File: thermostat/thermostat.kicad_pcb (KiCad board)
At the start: 2 copper layers, 13 parts, among them J1 Wall connections, J2 UART, U1 ESP32-WROVER-E, U2 TPS5430DDA, U3 TPS62203DBV

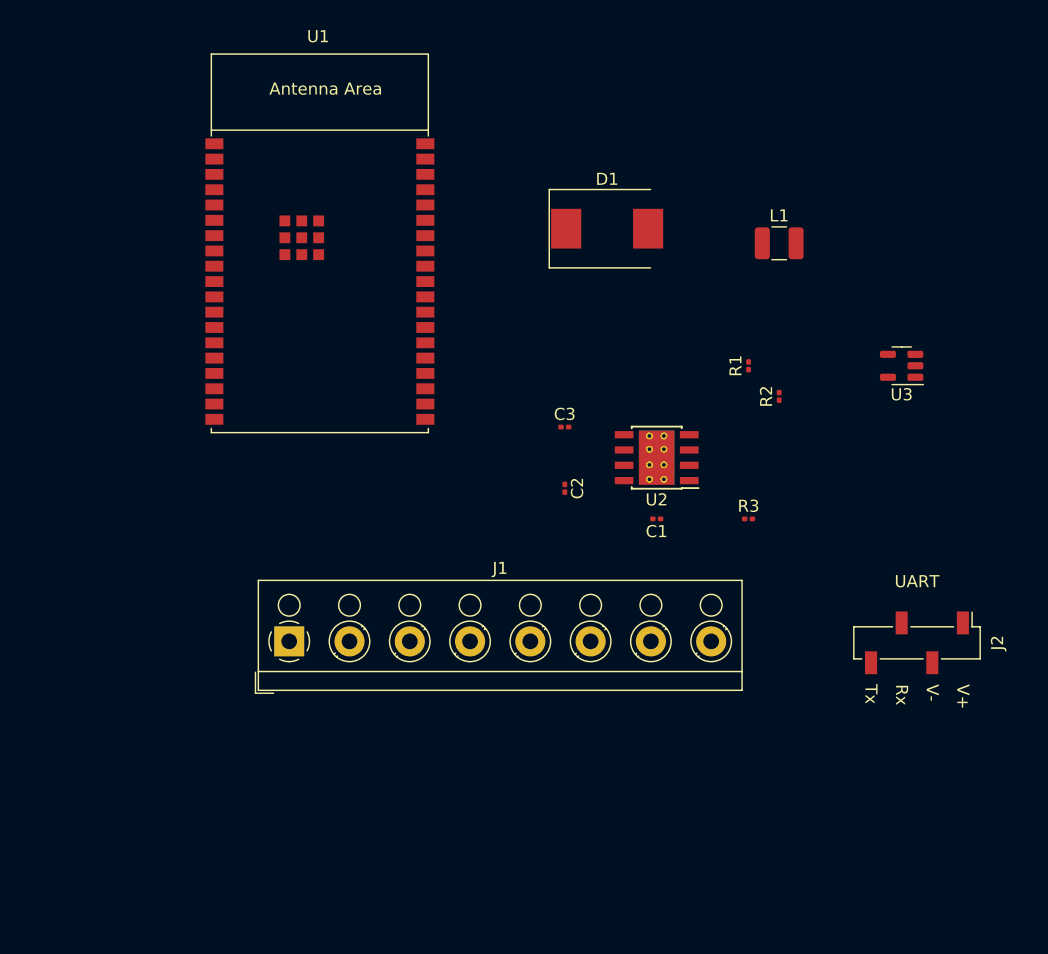
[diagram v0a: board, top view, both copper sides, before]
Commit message: update thermostat
I think I chose all the parts, just need to optimize the layout
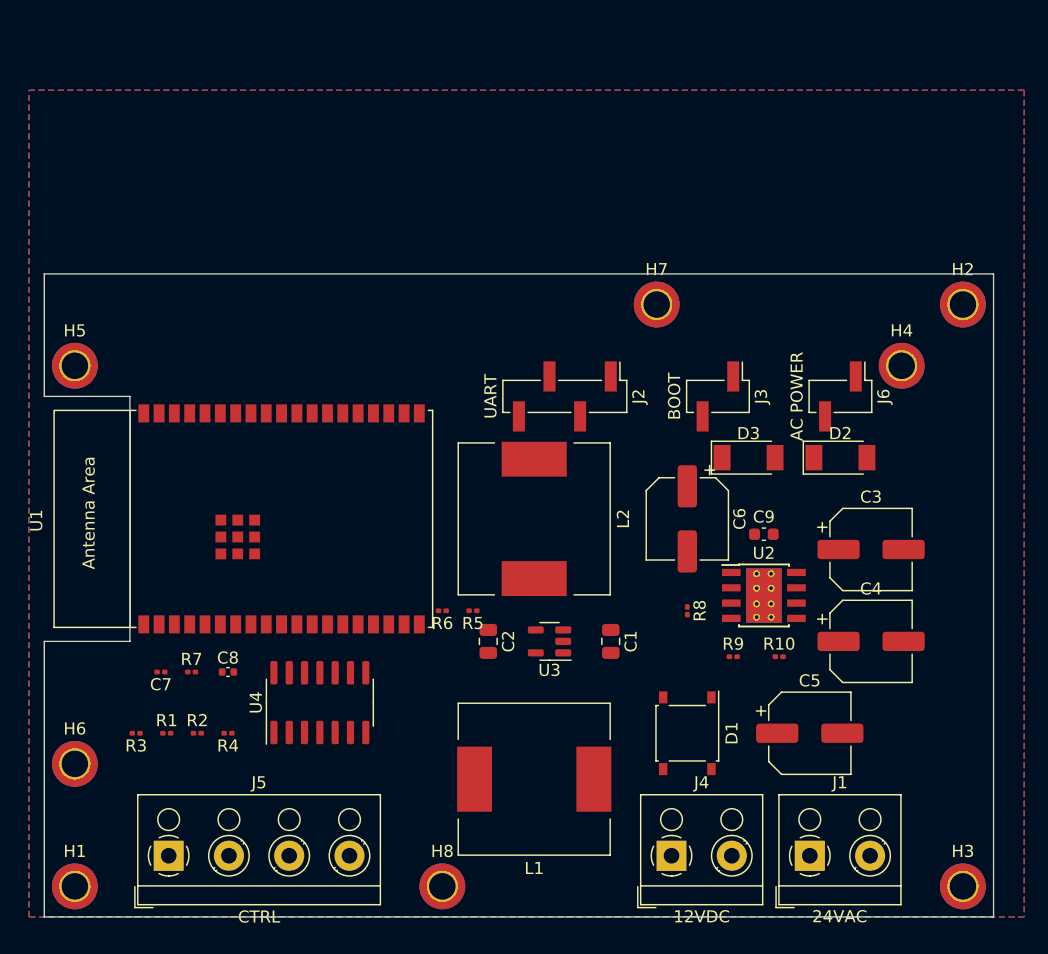
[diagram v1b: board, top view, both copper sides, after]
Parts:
- added C4: 470uF/50V, Capacitor_SMD:CP_Elec_6.3x7.7, F.Cu at (134.6, 121.9)
- added C5: 470uF/50V, Capacitor_SMD:CP_Elec_6.3x7.7, F.Cu at (129.5, 129.5)
- added C6: 100uF/25V, Capacitor_SMD:CP_Elec_6.3x7.7, F.Cu at (119.4, 111.8)
- added C7: 0.1uF/5V, Capacitor_SMD:C_0201_0603Metric, F.Cu at (75.7, 124.5)
- added C8: 1uF/5V, Capacitor_SMD:C_0402_1005Metric, F.Cu at (81.3, 124.5)
- added C9: 0.01uF, Capacitor_SMD:C_0603_1608Metric, F.Cu at (125.7, 113.0)
- added D2: SS34, Diode_SMD:D_SOD-128, F.Cu at (132.1, 106.7)
- added D3: SS34, Diode_SMD:D_SOD-128, F.Cu at (124.5, 106.7)
- added H1: MountingHole_Pad, MountingHole:MountingHole_2.2mm_M2_DIN965_Pad_TopBottom, F.Cu at (68.6, 142.2)
- added H2: MountingHole_Pad, MountingHole:MountingHole_2.2mm_M2_DIN965_Pad_TopBottom, F.Cu at (142.2, 94.0)
- added H3: MountingHole_Pad, MountingHole:MountingHole_2.2mm_M2_DIN965_Pad_TopBottom, F.Cu at (142.2, 142.2)
- added H4: MountingHole_Pad, MountingHole:MountingHole_2.2mm_M2_DIN965_Pad_TopBottom, F.Cu at (137.2, 99.1)
- added H5: MountingHole_Pad, MountingHole:MountingHole_2.2mm_M2_DIN965_Pad_TopBottom, F.Cu at (68.6, 99.1)
- added H6: MountingHole_Pad, MountingHole:MountingHole_2.2mm_M2_DIN965_Pad_TopBottom, F.Cu at (68.6, 132.1)
- added H7: MountingHole_Pad, MountingHole:MountingHole_2.2mm_M2_DIN965_Pad_TopBottom, F.Cu at (116.8, 94.0)
- added H8: MountingHole_Pad, MountingHole:MountingHole_2.2mm_M2_DIN965_Pad_TopBottom, F.Cu at (99.1, 142.2)
- added J3: BOOT, Connector_PinHeader_2.54mm:PinHeader_1x02_P2.54mm_Vertical_SMD_Pin1Left, F.Cu at (121.9, 101.6)
- added J4: 12VDC, TerminalBlock_RND:TerminalBlock_RND_205-00001_1x02_P5.00mm_Horizontal, F.Cu at (118.1, 139.7)
- added J5: CTRL, TerminalBlock_RND:TerminalBlock_RND_205-00003_1x04_P5.00mm_Horizontal, F.Cu at (76.4, 139.7)
- added J6: AC POWER, Connector_PinHeader_2.54mm:PinHeader_1x02_P2.54mm_Vertical_SMD_Pin1Left, F.Cu at (132.1, 101.6)
- added L2: YPRH1207-270M, Inductor_SMD:L_12x12mm_H8mm, F.Cu at (106.7, 111.8)
- added R10: 1.8k, Resistor_SMD:R_0201_0603Metric, F.Cu at (127.0, 123.2)
- added R4: 68k, Resistor_SMD:R_0201_0603Metric, F.Cu at (81.3, 129.5)
- added R5: 18k, Resistor_SMD:R_0201_0603Metric, F.Cu at (101.6, 119.4)
- added R6: 2k, Resistor_SMD:R_0201_0603Metric, F.Cu at (99.1, 119.4)
- added R7: 10k, Resistor_SMD:R_0201_0603Metric, F.Cu at (78.3, 124.5)
- added R8: 33k, Resistor_SMD:R_0201_0603Metric, F.Cu at (119.4, 119.4)
- added R9: 1.8k, Resistor_SMD:R_0201_0603Metric, F.Cu at (123.2, 123.2)
- added U4: LM324DT, Package_SO:SOIC-14_3.9x8.7mm_P1.27mm, F.Cu at (88.9, 127.0)
- C1: value 0.01uF -> 4.7 uF; footprint Capacitor_SMD:C_0201_0603Metric -> Capacitor_SMD:C_0805_2012Metric
- C2: value 10uF -> 10 uF; footprint Capacitor_SMD:C_0201_0603Metric -> Capacitor_SMD:C_0805_2012Metric
- C3: value 220uF -> 470uF/50V; footprint Capacitor_SMD:C_0201_0603Metric -> Capacitor_SMD:CP_Elec_6.3x7.7
- D1: value B340 -> ABS2; footprint Diode_SMD:D_SMC -> Diode_SMD:Diode_Bridge_Diotec_ABS
- J1: value Wall connections -> 24VAC; footprint TerminalBlock_RND:TerminalBlock_RND_205-00007_1x08_P5.00mm_Horizontal -> TerminalBlock_RND:TerminalBlock_RND_205-00001_1x02_P5.00mm_Horizontal
- J2: footprint Connector_PinSocket_2.54mm:PinSocket_1x04_P2.54mm_Vertical_SMD_Pin1Left -> Connector_PinHeader_2.54mm:PinHeader_1x04_P2.54mm_Vertical_SMD_Pin1Left
- L1: value 15uH -> YPRH1207-270M; footprint Inductor_SMD:L_1210_3225Metric -> Inductor_SMD:L_12x12mm_H8mm
- R1: value 10k -> 33k
- R2: value 1.37k -> 33k
- R3: value 20 -> 68k
- moved R1 57.1 mm to (76.2, 129.5), turned to 0 degrees
- moved R2 55.8 mm to (78.7, 129.5), turned to 0 degrees
- moved R3 53.8 mm to (73.7, 129.5), turned to 180 degrees
- moved L1 48.9 mm to (106.7, 133.3), turned to 180 degrees
- moved J1 46.7 mm to (129.5, 139.7)
- moved D1 42.4 mm to (119.4, 129.5), turned to -90 degrees
- moved U3 37.1 mm to (108.0, 121.9)
- moved J2 35.7 mm to (109.2, 101.6)
- moved C3 27.4 mm to (134.6, 114.3)
- moved U1 23.7 mm to (82.5, 111.8), turned to 90 degrees
- moved U2 14.5 mm to (125.7, 118.1), turned to 0 degrees
- moved C2 14.2 mm to (102.9, 121.9)
- moved C1 10.9 mm to (113.0, 121.9), turned to -90 degrees
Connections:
- C1 pad 1: Net-(C1-Pad1) -> /VCC12
- C1 pad 2: Net-(C1-Pad2) -> GND
- C2 pad 1: +12V -> /VCC33
- C3 pad 1: /VCC10 -> Net-(C3-Pad1)
- D1 pad 1: Net-(C1-Pad2) -> Net-(C3-Pad1)
- J1 pad 1: GND -> /VAC-
- J1 pad 2: +12V -> /VAC+
- J2 pad 1: /VCC33_IN -> /VCC33
- L1 pad 1: Net-(C1-Pad2) -> Net-(L1-Pad1)
- L1 pad 2: /VCC10 -> /VCC33
- R1 pad 2: /VCC10 -> GND
- R2 pad 1: Net-(R1-Pad1) -> Net-(R2-Pad1)
- R2 pad 2: Net-(R2-Pad2) -> GND
- R3 pad 1: Net-(R2-Pad2) -> Net-(R1-Pad1)
- R3 pad 2: GND -> /FAN_CTRL
- U1 pad 10: unconnected-(U1-Pad10) -> /GPIO25
- U1 pad 11: unconnected-(U1-Pad11) -> /GPIO26
- U1 pad 2: /VCC33_IN -> /VCC33
- U1 pad 25: unconnected-(U1-Pad25) -> /GPIO0
- U1 pad 3: unconnected-(U1-Pad3) -> /CHIP_PU
- U1 pad 35: unconnected-(U1-Pad35) -> /UART_TX
- U1 pad 4: unconnected-(U1-Pad4) -> /ADC1_CH0
- U2 pad 1: Net-(C1-Pad1) -> Net-(C9-Pad1)
- U2 pad 4: Net-(R1-Pad1) -> Net-(R8-Pad2)
- U2 pad 7: +12V -> Net-(C3-Pad1)
- U2 pad 8: Net-(C1-Pad2) -> Net-(C9-Pad2)
- U3 pad 1: +12V -> /VCC12
- U3 pad 3: unconnected-(U3-Pad3) -> /VCC12
- U3 pad 4: unconnected-(U3-Pad4) -> /VCC33
- U3 pad 5: unconnected-(U3-Pad5) -> Net-(L1-Pad1)
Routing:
- added copper zone on B.Cu, net GND
- added copper zone on F.Cu, net GND
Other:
- board outline added: 78.7 x 53.3 mm
- board text removed: "UART"

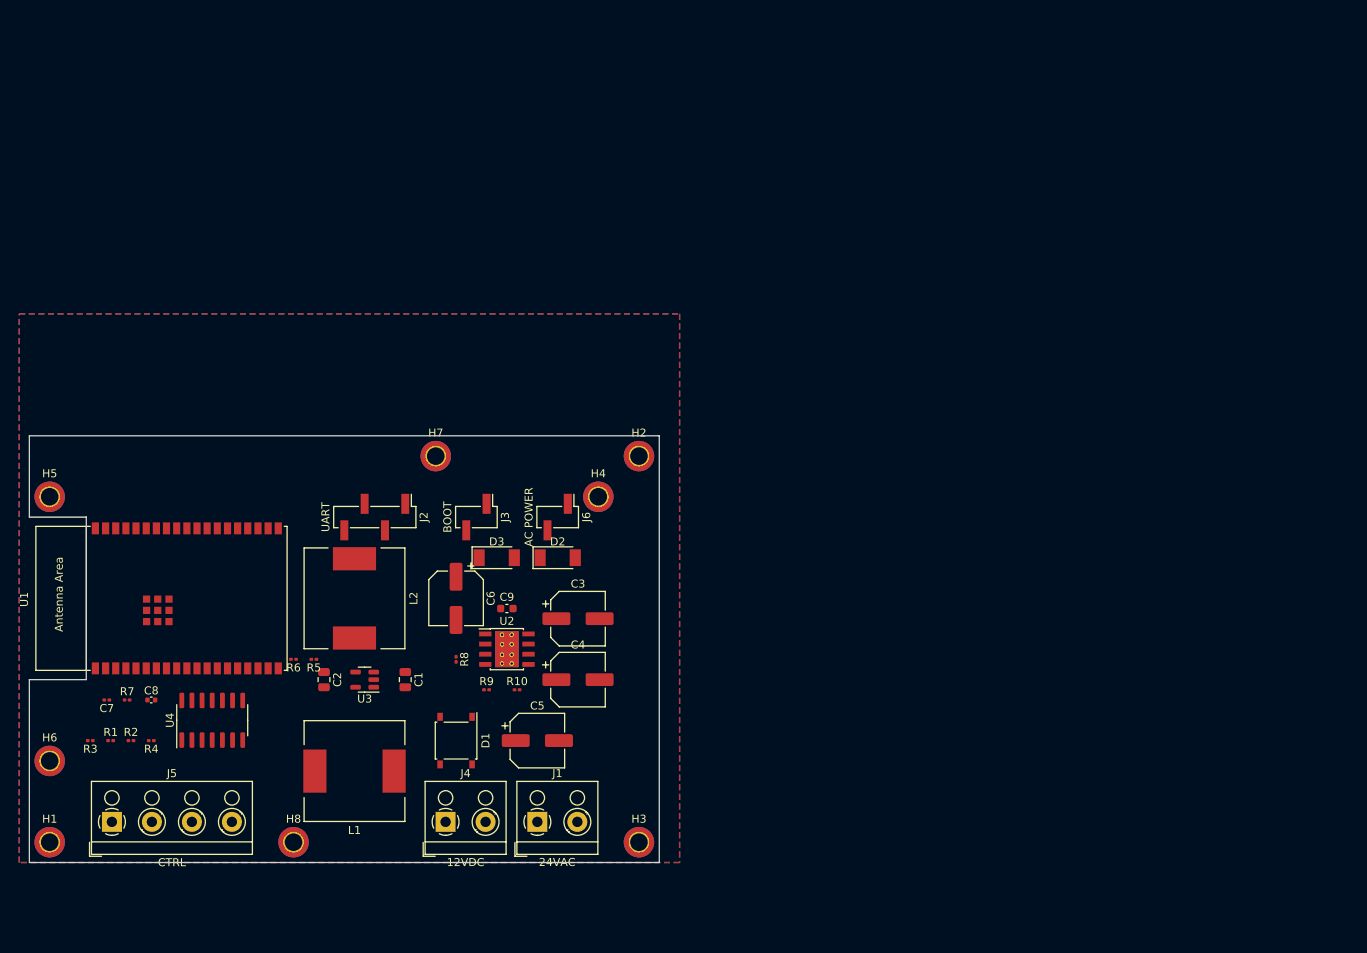
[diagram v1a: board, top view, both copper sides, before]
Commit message: layout with holes to fit in old slot
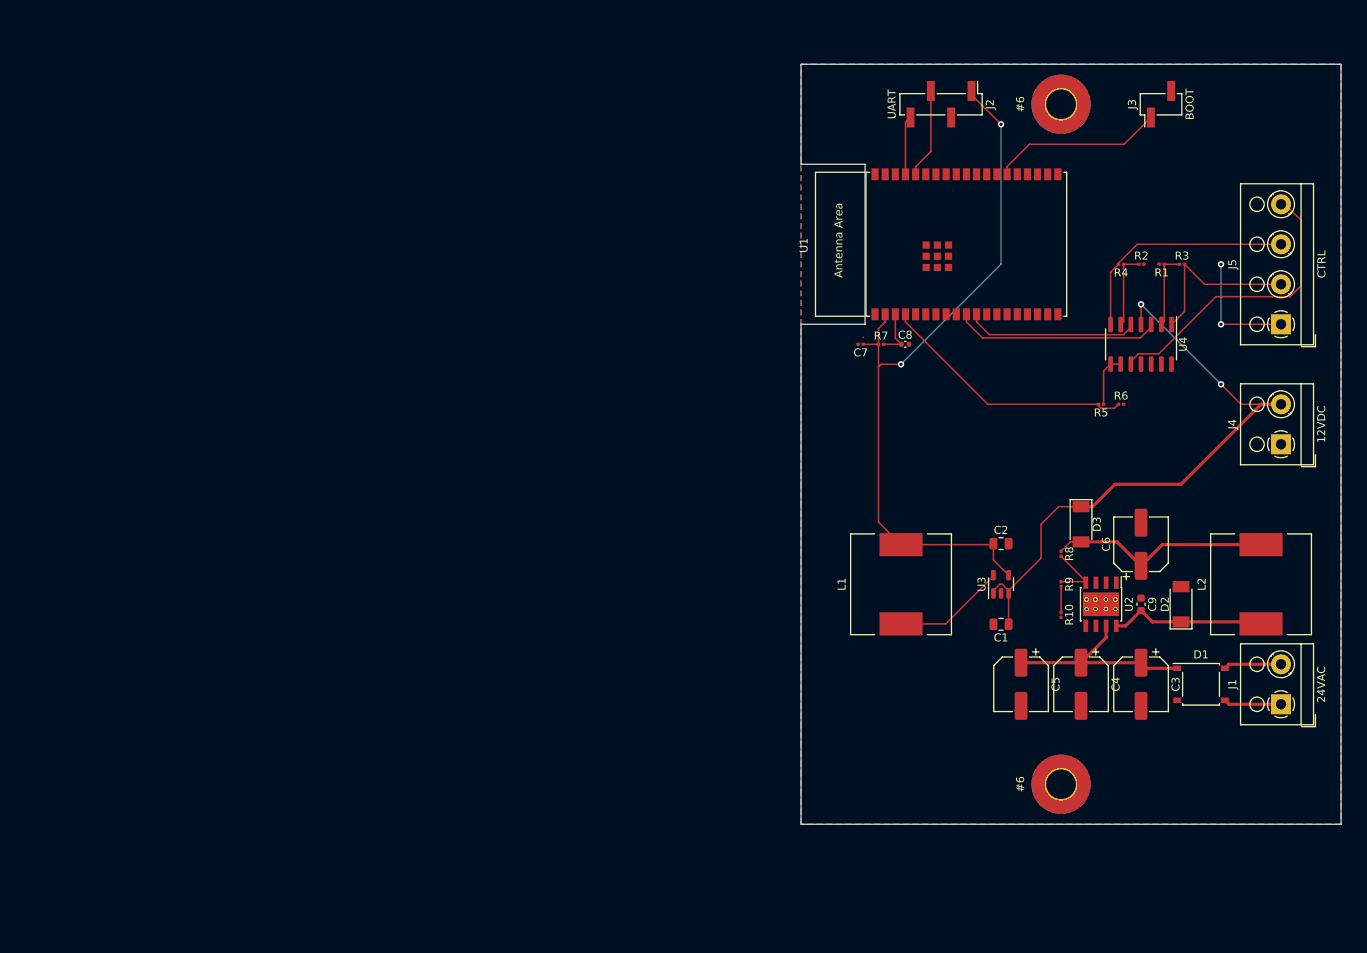
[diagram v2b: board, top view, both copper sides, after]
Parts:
- removed H3, H4, H5, H6, H7, H8: MountingHole_Pad, MountingHole:MountingHole_2.2mm_M2_DIN965_Pad_TopBottom
- removed J6: AC POWER, Connector_PinHeader_2.54mm:PinHeader_1x02_P2.54mm_Vertical_SMD_Pin1Left
- H1, H2: footprint MountingHole:MountingHole_2.2mm_M2_DIN965_Pad_TopBottom -> kelvie:MountingHole_No6_Pad_TopBottom
- moved J5 158.8 mm to (222.5, 77.5), turned to 90 degrees
- moved R3 148.9 mm to (210.1, 70.0), turned to 0 degrees
- moved R1 144.2 mm to (207.6, 70.0), turned to 180 degrees
- moved R2 139.6 mm to (205.0, 70.0)
- moved R4 135.1 mm to (202.5, 70.0)
- moved H1 126.6 mm to (195.0, 135.0), turned to 90 degrees
- moved U4 125.3 mm to (205.0, 80.0), turned to -90 degrees
- moved J4 114.6 mm to (222.5, 92.5), turned to 90 degrees
- moved L2 113.3 mm to (220.0, 110.0), turned to 90 degrees
- moved R6 108.2 mm to (202.5, 87.5), turned to 0 degrees
- moved U1 107.0 mm to (180.0, 67.5)
- moved C7 104.2 mm to (170.0, 80.0)
- moved C8 104.2 mm to (175.5, 80.0)
- moved R7 104.2 mm to (172.5, 80.0)
- moved R5 103.4 mm to (200.0, 87.5)
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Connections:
- net /GPIO25 renamed /DAC_1
- net /GPIO26 renamed /DAC_2
- D3 pad 1: /AC_JUMPER -> /VCC12
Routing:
- net /VCC33: track 0.00 -> 92.4 mm, vias 0 -> 2
- net /VCC12: track 0.00 -> 76.0 mm, vias 0 -> 2
- net /PUMP_TEMP: track 0.00 -> 36.9 mm
- net /ADC1_CH0: track 0.00 -> 32.3 mm
- net /PUMP_CTRL: track 0.00 -> 29.9 mm
- net Net-(C6-Pad1): track 0.00 -> 27.8 mm
- net /DAC_1: track 0.00 -> 25.8 mm
- net Net-(C3-Pad1): track 0.00 -> 25.7 mm
- net /FAN_CTRL: track 0.00 -> 21.8 mm
- net /DAC_2: track 0.00 -> 21.6 mm
- net /GPIO0: track 0.00 -> 21.5 mm
- net Net-(C9-Pad2): track 0.00 -> 19.6 mm
- net GND: track 0.00 -> 16.0 mm, vias 0 -> 2
- net Net-(L1-Pad1): track 0.00 -> 14.1 mm
- net /UART_RX: track 0.00 -> 11.2 mm
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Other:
- board size 78.7 x 53.3 mm -> 67.5 x 95 mm
